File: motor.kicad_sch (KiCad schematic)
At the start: 20 parts, among them J201 JST-SH, J202 JST-SH, J203 JST-SH, J204 JST-SH, U201 A4950E, U202 A4950E, U203 A4950E, U204 A4950E

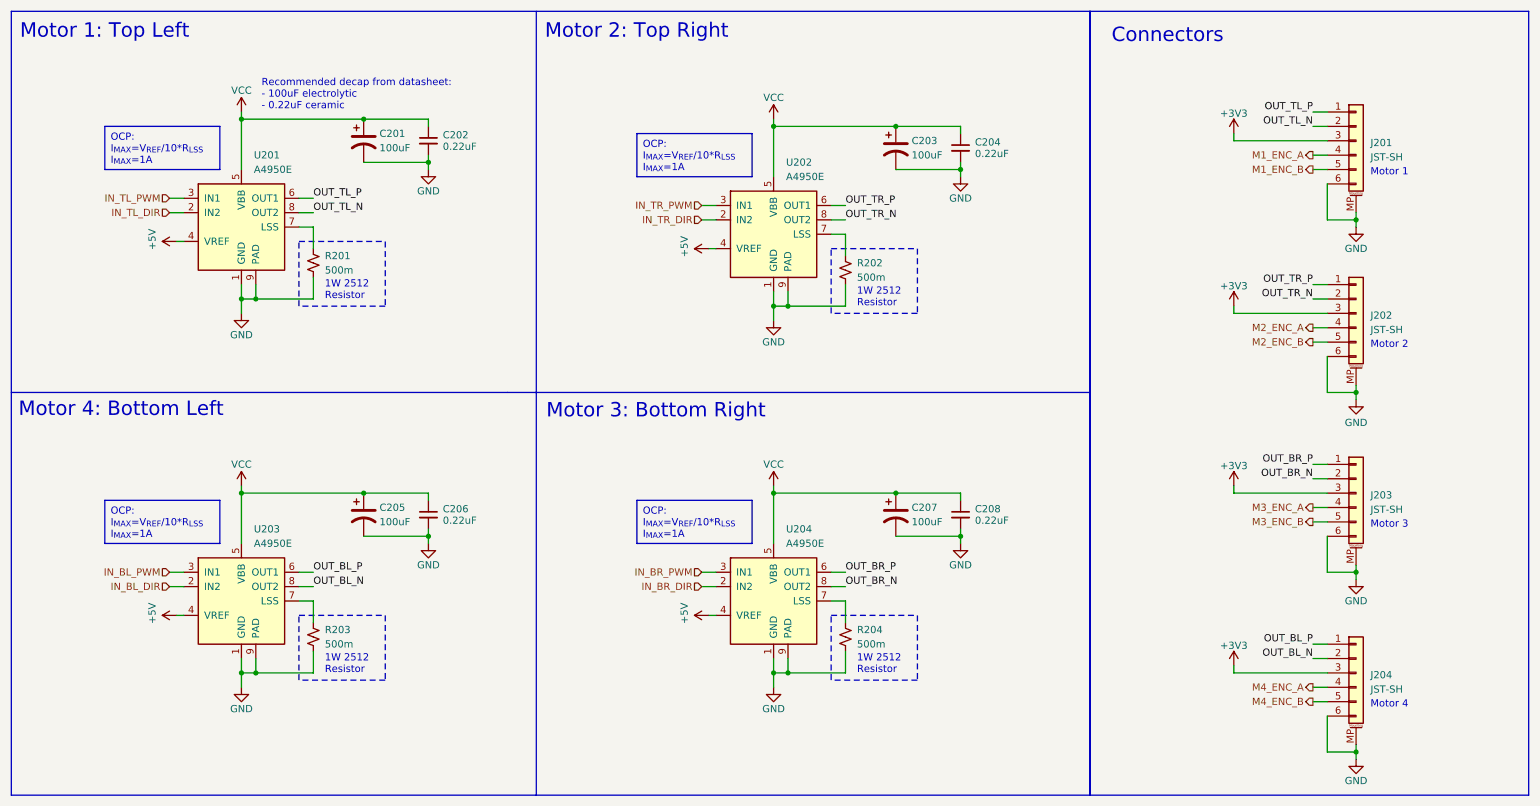
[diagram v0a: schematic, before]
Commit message: changed dimension of current sense resistor
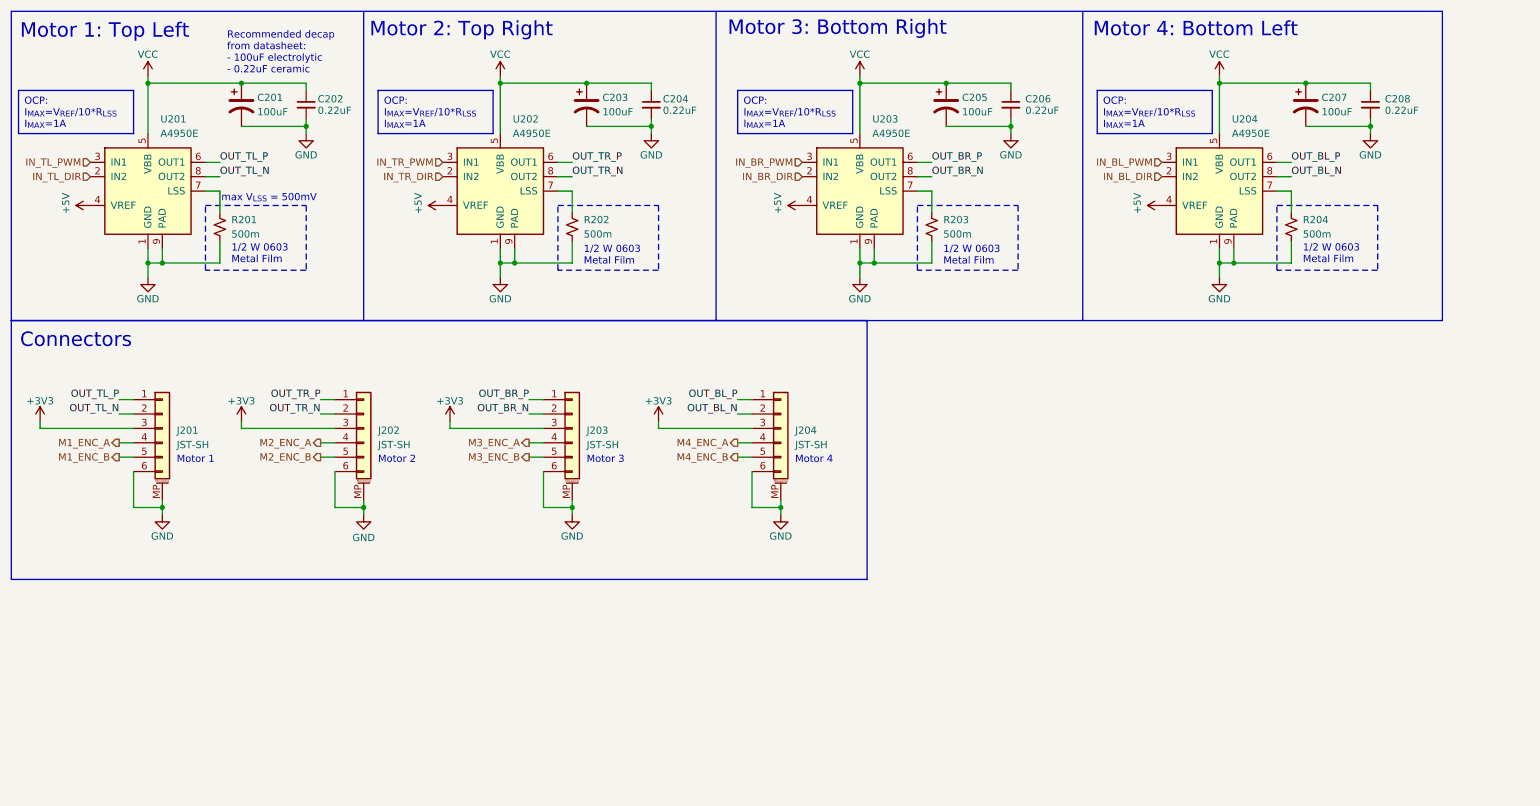
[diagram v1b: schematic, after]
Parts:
- R201, R202: footprint Resistor_SMD:R_2512_6332Metric -> Resistor_SMD:R_0603_1608Metric
- R203: renamed from R204; footprint Resistor_SMD:R_2512_6332Metric -> Resistor_SMD:R_0603_1608Metric
- R204: renamed from R203; footprint Resistor_SMD:R_2512_6332Metric -> Resistor_SMD:R_0603_1608Metric
- U201, U202: footprint Package_SO:SOIC-8-1EP_3.9x4.9mm_P1.27mm_EP2.41x3.3mm -> Package_SO:SOIC-8-1EP_3.9x4.9mm_P1.27mm_EP2.41x3.3mm_ThermalVias
- U203: renamed from U204; footprint Package_SO:SOIC-8-1EP_3.9x4.9mm_P1.27mm_EP2.41x3.3mm -> Package_SO:SOIC-8-1EP_3.9x4.9mm_P1.27mm_EP2.41x3.3mm_ThermalVias
- U204: renamed from U203; footprint Package_SO:SOIC-8-1EP_3.9x4.9mm_P1.27mm_EP2.41x3.3mm -> Package_SO:SOIC-8-1EP_3.9x4.9mm_P1.27mm_EP2.41x3.3mm_ThermalVias
- renumbered C207 to C205, C208 to C206, C205 to C207, C206 to C208
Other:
- note added: "1/2 W 0603 Metal Film"
- note added: "max V_{LSS} = 500mV"
- note removed: "1W 2512 Resistor"
- moved on the sheet: C201, C202, C203, C204, C205, C206, C207, C208, J201, J202, J203, J204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

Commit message: version 2 done
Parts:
- removed C203, C205, C207: 100uF, Capacitor_SMD:CP_Elec_6.3x7.7, symbol Device:C_Polarized_US
- removed C204, C206, C208: 0.22uF, Capacitor_SMD:C_0603_1608Metric, symbol Device:C_Small
- removed J202, J203, J204: JST-SH, Connector_JST:JST_SH_SM06B-SRSS-TB_1x06-1MP_P1.00mm_Horizontal, symbol Connector_Generic_MountingPin:Conn_01x06_MountingPin
- removed R202, R203, R204: 500m, Resistor_SMD:R_0603_1608Metric, symbol Device:R_Small_US
- removed U202, U203, U204: A4950E, Package_SO:SOIC-8-1EP_3.9x4.9mm_P1.27mm_EP2.41x3.3mm_ThermalVias, symbol Driver_Motor:A4950E
- added R31: 200k, Resistor_SMD:R_0402_1005Metric, symbol Device:R_Small_US
- added R32: 50k, Resistor_SMD:R_0402_1005Metric, symbol Device:R_Small_US
- J9: renamed from J201; value JST-SH -> BM06B-SRSS-TB; footprint Connector_JST:JST_SH_SM06B-SRSS-TB_1x06-1MP_P1.00mm_Horizontal -> Connector_JST:JST_SH_BM06B-SRSS-TB_1x06-1MP_P1.00mm_Vertical
- R33: renamed from R201; value 500m -> RL10FTNR100; footprint Resistor_SMD:R_0603_1608Metric -> Resistor_SMD:R_0805_2012Metric
- renumbered C201 to C35, C202 to C36, U201 to U8
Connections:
- net +5V: now also R31.2; no longer U8.4 (VREF)
- net GND: now also R32.1
- net IN_TL_DIR renamed PWM_B
- net IN_TL_PWM renamed PWM_A
- net M1_ENC_A renamed ENC_A
- net M1_ENC_B renamed ENC_B
- net OUT_TL_N renamed OUT_N
- net OUT_TL_P renamed OUT_P
- new net: R31.1, R32.2, U8.4 (VREF)
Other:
- note added: "100m"
- note added: "500mW 0805 Metal Film"
- note added: "Motor Driver"
- note added: "Note: max V_{LSS} = 500mV"
- note added: "V_{LSS} ~ 100mV"
- note added: "V_{REF}=1V"
- note removed: "1/2 W 0603 Metal Film"
- note removed: "Motor 1"
- note removed: "Motor 1: Top Left"
- note removed: "Motor 2"
- note removed: "Motor 2: Top Right"
- note removed: "Motor 3"
- note removed: "Motor 3: Bottom Right"
- note removed: "Motor 4"
- note removed: "Motor 4: Bottom Left"
- note removed: "max V_{LSS} = 500mV"
- moved on the sheet: C35, C36, J9, R33, U8

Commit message: last modification for v2.0 before submitting order
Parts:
- R28: renamed from R32; value 50k -> 51k
- renumbered R31 to R27, R33 to R29, U8 to U10
